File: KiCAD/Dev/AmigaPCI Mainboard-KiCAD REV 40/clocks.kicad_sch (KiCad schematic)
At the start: 49 parts, among them U1 74LVC1G17, U108 74AHC04, U210 AT27C4096, U211 AT27C4096, U219 74AHCT04, U230 74LVC1G157, U812 SN74LVC16T245DLR, U813 SN74LVC16T245DLR, U814 74LVC245, U815 74LVC08, U816 74LVC245, U817 74LVC245, X1 6MHz, X2 33MHz, X3 20MHz, X4 28.63636MHz

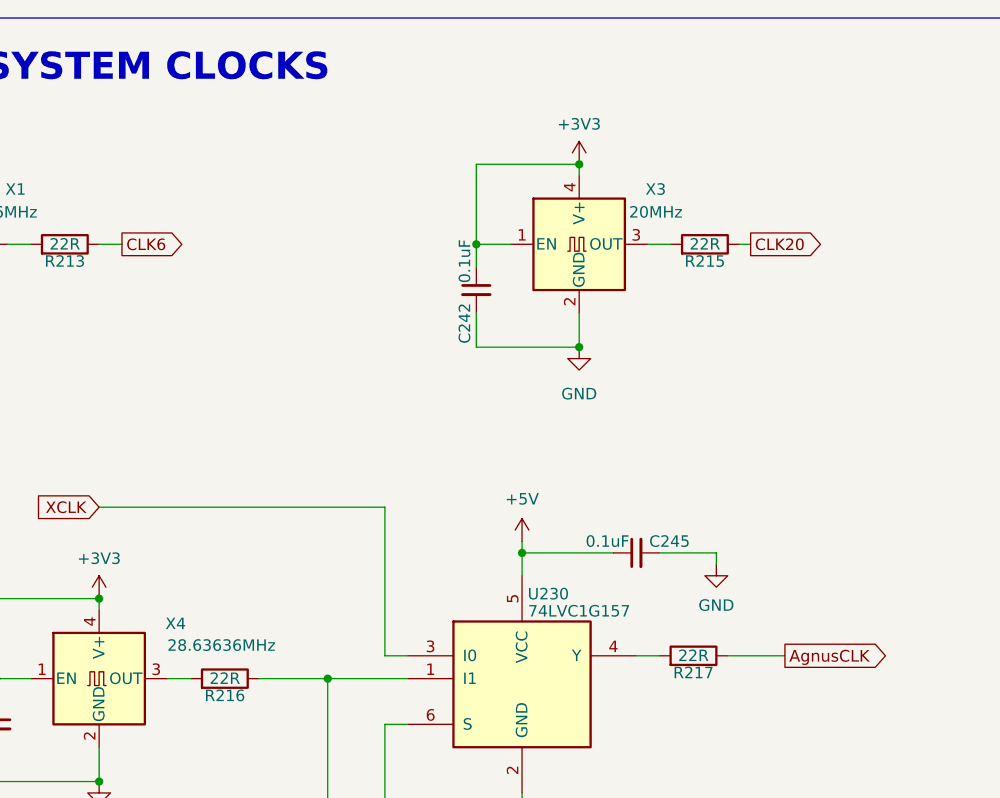
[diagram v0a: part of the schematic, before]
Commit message: Schematic Changes to Clocks 09-JUL-2024
Make changes to support clock generation on CPU local bus card.
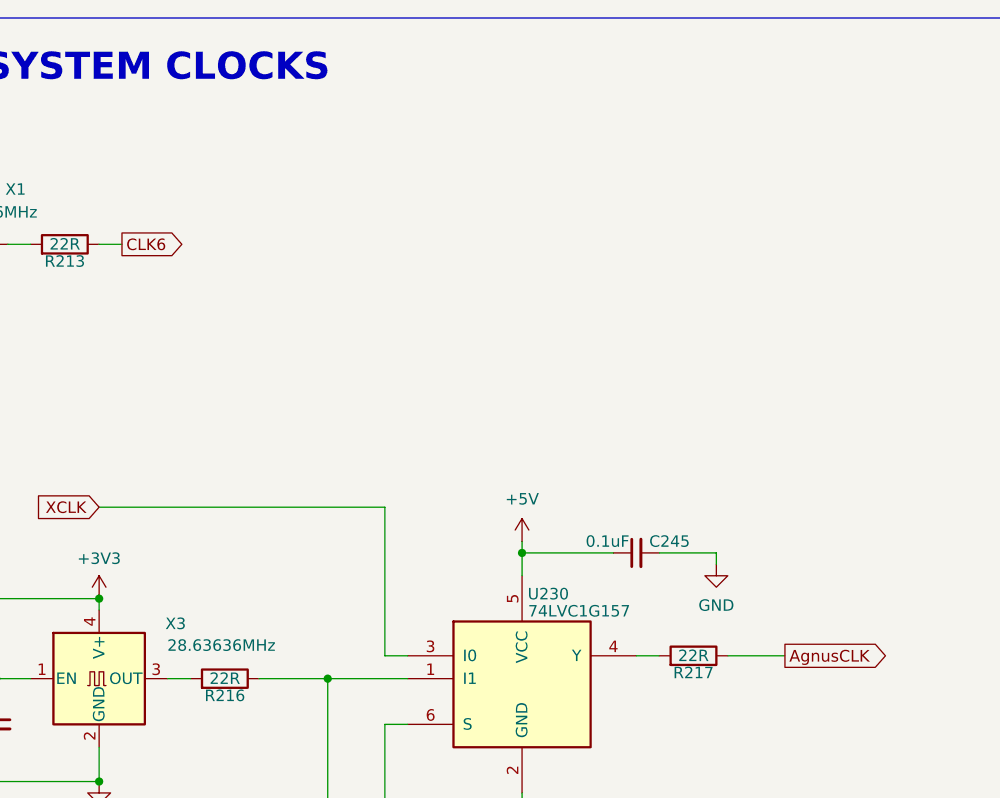
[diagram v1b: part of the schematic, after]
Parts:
- removed C242: 0.1uF, Capacitor_SMD:C_0603_1608Metric, symbol Device:C_Small
- removed R215: 22R, Resistor_SMD:R_0603_1608Metric, symbol Device:R
- removed X3: 20MHz, Oscillator:Oscillator_SMD_ECS_2520MV-xxx-xx-4Pin_2.5x2.0mm, symbol Oscillator:XO32
- renumbered X4 to X3

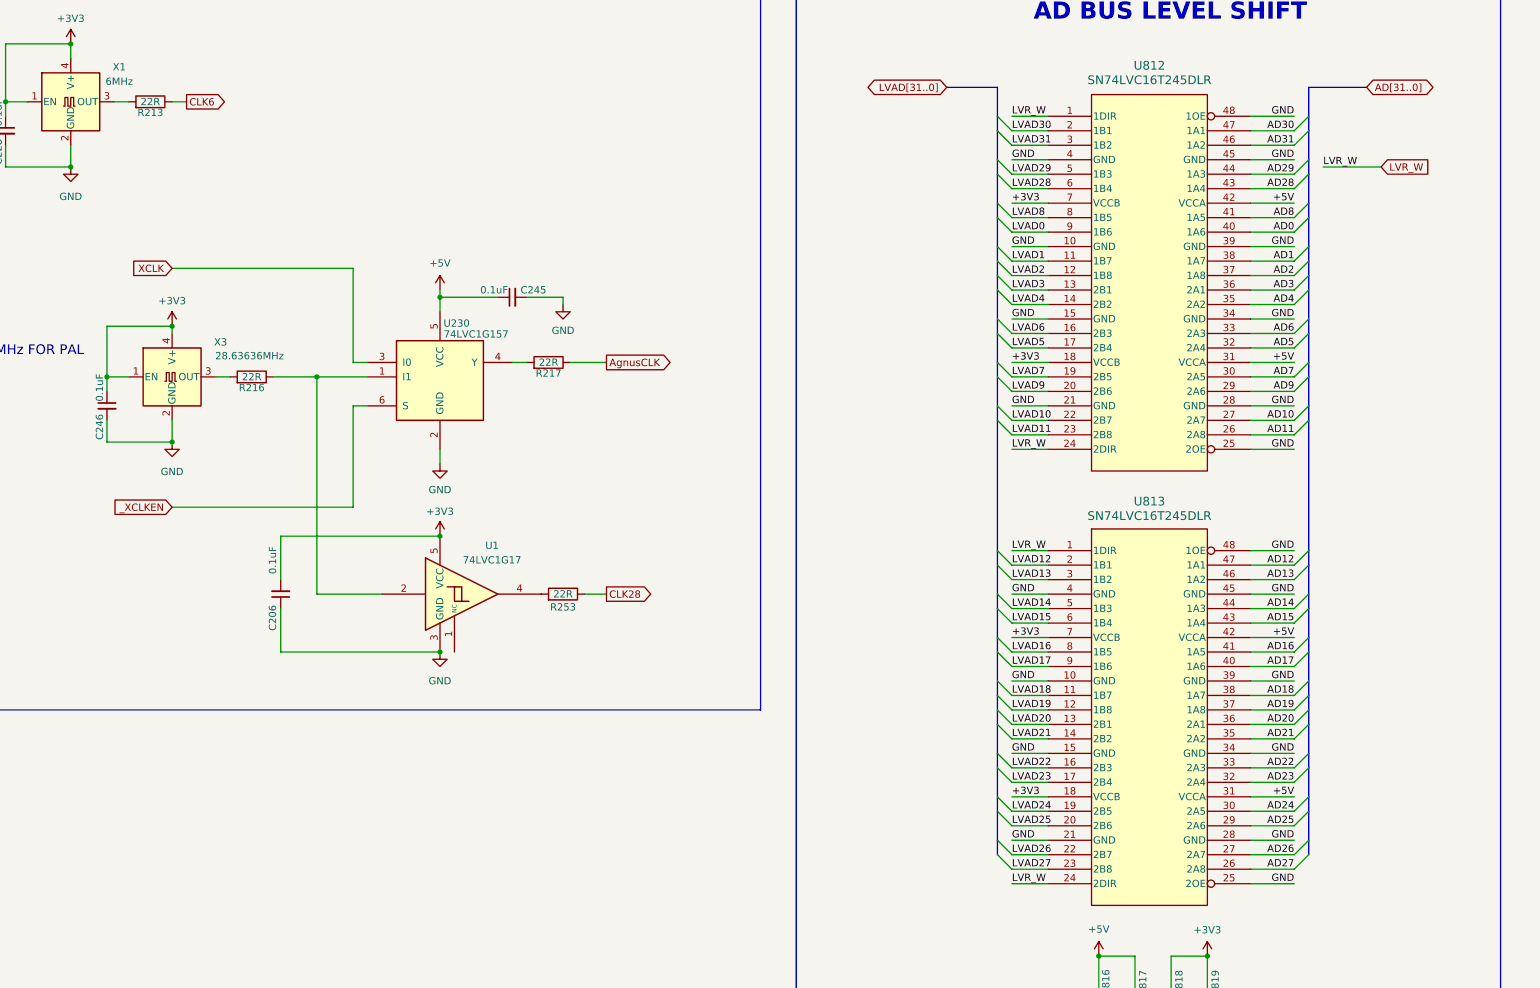
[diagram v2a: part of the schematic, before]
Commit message: AmigaPCI Rev 4.0 Routing
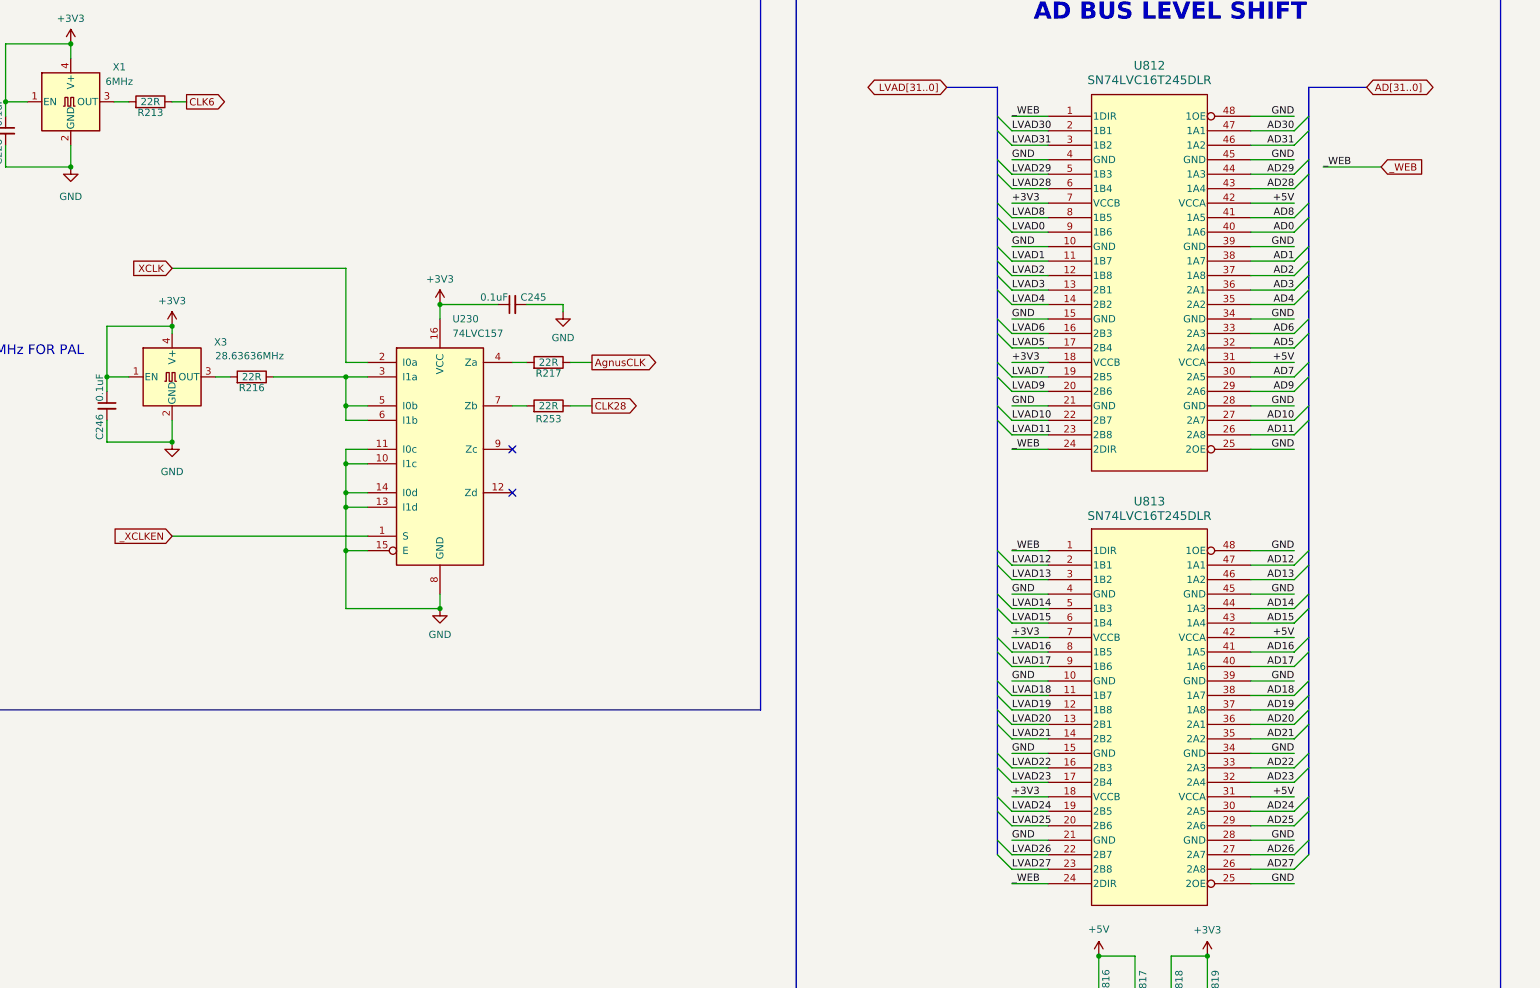
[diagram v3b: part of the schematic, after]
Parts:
- removed C206: 0.1uF, Capacitor_SMD:C_0603_1608Metric, symbol Device:C_Small
- removed U1: 74LVC1G17, Package_TO_SOT_SMD:SOT-23-5, symbol 74xGxx:74LVC1G17
- removed U230: 74LVC1G157, Package_SO:TSOP-6_1.65x3.05mm_P0.95mm, symbol AmigaPCI-Symbols:74LVC1G157
- added U230: 74LVC157, Package_SO:TSSOP-16_4.4x5mm_P0.65mm, symbol 74xx:74LS157
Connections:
- net +3V3: now also C245.1, U230.16 (VCC)
- net +5V: no longer C245.1
- net GND: now also U230.10 (I1c), U230.11 (I0c), U230.13 (I1d), U230.14 (I0d), U230.15 (E), U230.8 (GND)
- net XCLK: now also U230.2 (I0a)
- net _XCLKEN: now also U230.1 (S)
- net at R253.2: now also U230.7 (Zb)
- net at R216.1: now also U230.3 (I1a), U230.5 (I0b), U230.6 (I1b)
- net at R217.2: now also U230.4 (Za)
- net LVR_W renamed _WEB
- no-connect marks 0 -> 2
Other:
- moved on the sheet: C245, R253
